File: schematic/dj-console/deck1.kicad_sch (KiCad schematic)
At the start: 111 parts, among them Q1 BC547, Q10 BC547, Q11 BC547, Q2 BC547, Q3 BC547, Q4 BC547, Q5 BC547, Q6 BC547, Q7 BC547, Q8 BC547, Q9 BC547, SW1_1 SW_Push, SW2_1 SW_Push, SW3_1 SW_Push, SW4_1 SW_Push, U2 MCP23017_SP, x1/2_IN_SW1 SW_Push, x2_OUT_SW1 SW_Push

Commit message: Added CD4013B to schematic
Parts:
- added U1, U3: ~, symbol D-flipflop:CD4013B
- C10, C12, C13, C14, C8, C9: value 1nF -> C
- R1: renamed from Rc1; value 520 -> R
- R1: renamed from Rb1; value 43kohm -> R
- R1, R11, R13, R3, R5, R7, R9: value 100k -> 100kOhm
- R10: renamed from Rc10; value 520 -> R
- R10, R12, R2, R4, R6, R8: value 12k -> 12kOhm
- R10: renamed from Rb10; value 43kohm -> R
- R11: renamed from Rb11; value 43kohm -> R
- R11: renamed from Rc11; value 520 -> R
- R14: value 12k -> 1nF
- R15, R17, R19, R23, R25, R27: value 100k -> R
- R16, R18, R20, R24, R26, R28: value 12k -> R
- R2: renamed from Rb2; value 43kohm -> R
- R2: renamed from Rc2; value 520 -> R
- R3: renamed from Rc3; value 520 -> R
- R3: renamed from Rb3; value 43kohm -> R
- R4: renamed from Rc4; value 520 -> R
- R4: renamed from Rb4; value 43kohm -> R
- R5: renamed from Rc5; value 520 -> R
- R5: renamed from Rb5; value 43kohm -> R
- R6: renamed from Rb6; value 43kohm -> R
- R6: renamed from Rc6; value 520 -> R
- R7: renamed from Rb7; value 43kohm -> R
- R7: renamed from Rc7; value 520 -> R
- R8: renamed from Rb8; value 43kohm -> R
- R8: renamed from Rc8; value 520 -> R
- R9: renamed from Rb9; value 43kohm -> R
- R9: renamed from Rc9; value 520 -> R
- SW2: renamed from CUE_SW1; value SW_Push -> CUE_SW1
- renumbered STEMS_SW1 to SW1, SYNC_SW1 to SW1, LOOP_SW1 to SW1, HOTCUE_SW1 to SW1, SHIFT_SW1 to SW1, x1/2_IN_SW1 to x1/2_IN_SW?, x2_OUT_SW1 to x2_OUT_SW?
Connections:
- net GND: now also U1.7 (VSS), U3.7 (VSS)
- net PLAY_SW1: now also U1.3 (CLK1), U3.3 (CLK1)
- net SYNC_SW1: now also U1.11 (CLK2), U3.11 (CLK2)
- new net PLAY_LED1: U1.1 (Q1), U3.1 (Q1)
- new net SYNC_LED1: U1.13 (Q2), U3.13 (Q2)
- new net ~{PLAY_LED1}: U1.2 (~{Q1}), U1.5 (D1), U3.2 (~{Q1}), U3.5 (D1)
- new net ~{SYNC_LED1}: U1.12 (~{Q2}), U1.9 (D2), U3.12 (~{Q2}), U3.9 (D2)
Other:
- note added: "Vce = 1V Ib = 100uA Ic = 20mA Rb = 43kohm Rc = 510"
- note removed: "Vce = 1V Ib = 100uA Ic = 20mA"
- moved on the sheet: C12, C13, C14, C8, D12, D13, D14, D8, R15, R16, R23, R24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

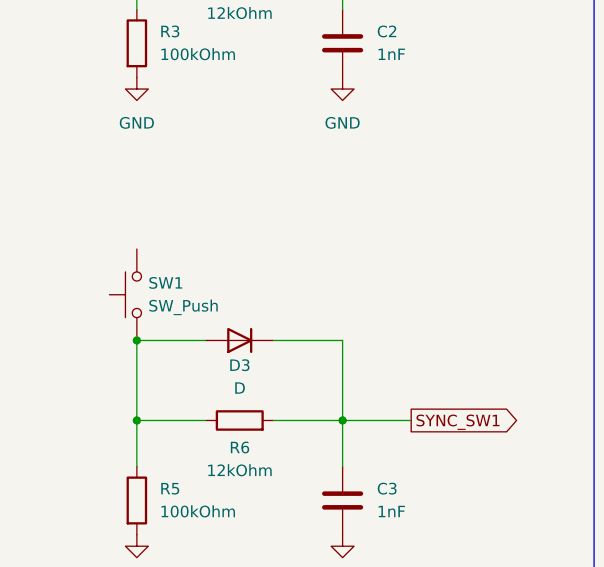
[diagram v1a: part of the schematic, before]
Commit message: Added CD4013B to schematic
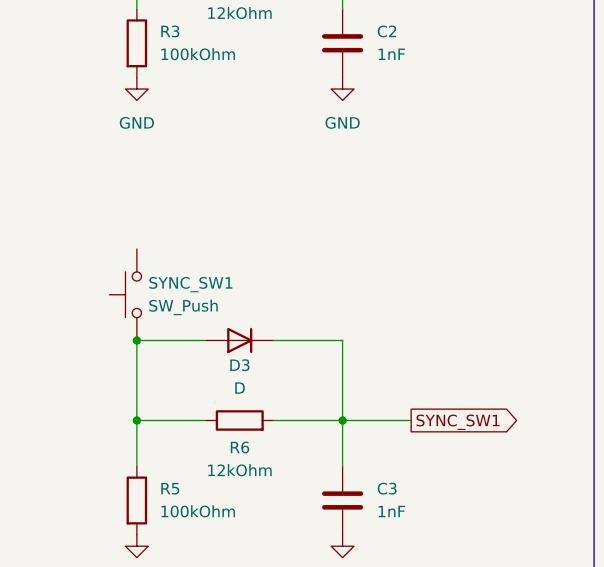
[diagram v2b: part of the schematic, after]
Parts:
- renumbered SW1 to SYNC_SW1
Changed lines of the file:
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@@
 		(dnp no)
 		(fields_autoplaced yes)
-		(property "Reference" "SW1"
+		(property "Reference" "SYNC_SW1"
 			(at 26.67 130.8099 90)
 			(effects
@@
 			(project "dj-console"
 				(path "/cbea8acf-e301-41c4-99fc-3eb7e47427af/a354910e-06bf-4bdc-8f1b-b82fc8536ab6"
-					(reference "SW1")
+					(reference "SYNC_SW1")
 					(unit 1)
 				)
@@
 		(dnp no)
 		(fields_autoplaced yes)
-		(property "Reference" "#PWR?"
+		(property "Reference" "#PWR0101"
 			(at 427.99 58.42 0)
 			(effects
@@
 			(project "dj-console"
 				(path "/cbea8acf-e301-41c4-99fc-3eb7e47427af/a354910e-06bf-4bdc-8f1b-b82fc8536ab6"
-					(reference "#PWR?")
+					(reference "#PWR0101")
 					(unit 1)
 				)
@@
 		(dnp no)
 		(fields_autoplaced yes)
-		(property "Reference" "#PWR?"
+		(property "Reference" "#PWR0102"
 			(at 427.99 100.33 0)
 			(effects
@@
 			(project "dj-console"
 				(path "/cbea8acf-e301-41c4-99fc-3eb7e47427af/a354910e-06bf-4bdc-8f1b-b82fc8536ab6"
-					(reference "#PWR?")
+					(reference "#PWR0102")
 					(unit 1)
 				)

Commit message: Connected switches for PADs controls to DFFs
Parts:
- removed U2: MCP23017_SP, Package_DIP:DIP-28_W7.62mm, symbol Interface_Expansion:MCP23017_SP
- added U4: MCP23017x-x-SP, Package_DIP:DIP-28_W7.62mm, symbol Interface_Expansion:MCP23017x-x-SP
- added U5, U6, U7: (no value), symbol D-flipflop:CD4013B
- U1, U3: value ~ -> (none)
- gave numbers to parts that had none: 2
- renumbered SW1 to HOT_CUE_SW1, SW1 to STEMS_SW1, SW2 to SW_Push, SW1 to x1-2_SW1, SW1 to x2_SW1
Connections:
- net CUE_SW1: now also U4.23 (GPA2)
- net GND: now also U4.10 (V_{SS}), U5.7 (VSS), U6.7 (VSS), U7.7 (VSS)
- net PLAY_LED1: now also U4.21 (GPA0), U7.1 (Q1); no longer U3.1 (Q1)
- net PLAY_SW1: now also U7.3 (CLK1); no longer U3.3 (CLK1)
- net SYNC_LED1: now also U4.22 (GPA1), U7.13 (Q2); no longer U3.13 (Q2)
- net SYNC_SW1: now also U7.11 (CLK2); no longer U3.11 (CLK2)
- net ~{PLAY_LED1}: now also U7.2 (~{Q1}), U7.5 (D1); no longer U3.2 (~{Q1}), U3.5 (D1)
- net ~{SYNC_LED1}: now also U7.12 (~{Q2}), U7.9 (D2); no longer U3.12 (~{Q2}), U3.9 (D2)
- net x2_SW1: now reaches C8.1, D8.1 (K), R16.2
- net x2_SW1: now also U6.11 (CLK2)
- net x1-2_SW1: now reaches C14.1, D14.1 (K), R28.2
- net x1-2_SW1: now also U6.3 (CLK1)
- net STEMS_SW1: now reaches C13.1, D13.1 (K), R26.2
- net STEMS_SW1: now also U5.11 (CLK2)
- net SHIFT_SW1: now reaches C10.1, D10.1 (K), R20.2
- net SHIFT_SW1: now also U3.11 (CLK2)
- net LOOP_SW1: now reaches C9.1, D9.1 (K), R18.2
- net LOOP_SW1: now also U3.3 (CLK1)
- net HOT_CUE_SW1: now reaches C12.1, D12.1 (K), R24.2
- net HOT_CUE_SW1: now also U5.3 (CLK1)
- new net HOT_CUE_LED1: U5.1 (Q1)
- new net LOOP_LED1: U3.1 (Q1)
- new net SHIFT_LED1: U3.13 (Q2)
- new net STEMS_LED1: U5.13 (Q2)
- new net x1-2_LED1: U6.1 (Q1)
- new net x2_LED1: U6.13 (Q2)
- new net ~{HOT_CUE_LED1}: U5.2 (~{Q1}), U5.5 (D1)
- new net ~{LOOP_LED1}: U3.2 (~{Q1}), U3.5 (D1)
- new net ~{SHIFT_LED1}: U3.12 (~{Q2}), U3.9 (D2)
- new net ~{STEMS_LED1}: U5.12 (~{Q2}), U5.9 (D2)
- new net ~{x1-2_LED1}: U6.2 (~{Q1}), U6.5 (D1)
- new net ~{x2_LED1}: U6.12 (~{Q2}), U6.9 (D2)
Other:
- moved on the sheet: C10, C12, C13, C14, C8, C9, D10, D11, D12, D13, D14, D15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

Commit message: Finished DECK circuitry -> to be reviewed; Created hierarchical sheets to avoid redundancy
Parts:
- removed D19: LED, symbol Device:LED
- removed Q6: BC547, Package_TO_SOT_THT:TO-92_Inline, symbol Transistor_BJT:BC547
- removed R10 (x2), R11 (x2), R3 (x2), R4 (x2), R5 (x2), R6 (x2), R7 (x2), R8 (x2), R9 (x2): R, symbol Device:R
- removed U7: (no value), symbol D-flipflop:CD4013B
- added C10, C11, C12, C37, C8, C9: 10uF, symbol Device:C_Polarized
- added D15, D25, D26: LED, symbol Device:LED
- added Q12, Q13, Q2: BC547, Package_TO_SOT_THT:TO-92_Inline, symbol Transistor_BJT:BC547
- added R28, R29, R30, R35, R37, R41, R42, R43, R47, R48, R49: 43kOhm, symbol Device:R
- added R32, R33, R34, R38, R40, R44, R45, R46, R50, R51, R52: 510Ohm, symbol Device:R
- added U1: LM741, symbol Amplifier_Operational:LM741
- added U7: (no value), symbol GPIO_expander:MCP23017
- C13: renamed from C9; value C -> 1nF
- C14: renamed from C10; value C -> 1nF
- C15: renamed from C12; value C -> 1nF
- C16: renamed from C13; value C -> 1nF
- C17: renamed from C14; value C -> 1nF
- C18: renamed from C8; value C -> 1nF
- R15: renamed from R17; value R -> 100kOhm
- R16: renamed from R19; value R -> 100kOhm
- R17: renamed from R23; value R -> 100kOhm
- R18: renamed from R25; value R -> 100kOhm
- R19: renamed from R27; value R -> 10kOhm
- R20: renamed from R15; value R -> 100kOhm
- R21: renamed from R18; value R -> 12kOhm
- R22: renamed from R20; value R -> 12kOhm
- R23: renamed from R24; value R -> 12kOhm
- R24: renamed from R26; value R -> 12kOhm
- R25: renamed from R28; value R -> 12kOhm
- R26: renamed from R16; value R -> 12kOhm
- R27: renamed from R1; value R -> 43kOhm
- R31: renamed from R1; value R -> 510Ohm
- R36: renamed from R2; value R -> 43kOhm
- R39: renamed from R2; value R -> 510Ohm
- SW_Push: value CUE_SW1 -> CUE_SW
- renumbered D12 to D10, D13 to D11, D14 to D12, D8 to D13, D11 to D14, D15 to D19, D9 to D8, D10 to D9, Q2 to Q6, R6 to R10, R8 to R11, R10 to R12, R12 to R13, R3 to R2, R5 to R3, R7 to R4, R9 to R5, R11 to R6, R13 to R7, R2 to R8, R4 to R9, SW1_1 to SW1, SW2_1 to SW2, SW3_1 to SW3, SW4_1 to SW4, U4 to U2, U1 to U3, U3 to U4, U1 to U8
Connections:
- net HOT_CUE_LED1 is gone; now on net HOT_CUE_LED: U5.1 (Q1)
- net LOOP_LED1 is gone; now on net LOOP_LED: U4.1 (Q1)
- net PLAY_LED1 is gone; now on net PLAY_LED: U2.21 (GPA0), U3.1 (Q1)
- net SHIFT_LED1 is gone; now on net SHIFT_LED: U4.13 (Q2)
- net STEMS_LED1 is gone; now on net STEMS_LED: U5.13 (Q2)
- net SW2_1 is gone; now on net SW2: C5.1, D5.1 (K), R12.2
- net SW3_1 is gone; now on net SW3: C6.1, D6.1 (K), R13.2
- net SW4_1 is gone; now on net SW4: C7.1, D7.1 (K), R14.2
- net x1-2_LED1 is gone; now on net x1-2_LED: U6.1 (Q1)
- net x2_LED1 is gone; now on net x2_LED: U6.13 (Q2)
- net +12V: now also R32.1, R33.1, R34.1, R38.1, R40.1, R44.1, R45.1, R46.1, R50.1, R51.1, R52.1
- net GND: now also C10.2, C11.2, C12.2, C8.2, C9.2, Q12.3 (E), Q13.3 (E), Q2.3 (E), U1.4 (V-)
- net +5V: now reaches STEMS_SW1.2
- net +5V: now also HOT_CUE_SW1.2, LOOP_SW1.2, PLAY_SW1.2, SHIFT_SW1.2, SW1.2, SW2.2, SW3.2, SW4.2, SW_Push.2, SYNC_SW1.2, U2.9 (V_{DD}), U3.14 (VDD), U4.14 (VDD), U5.14 (VDD), U6.14 (VDD), x1-2_SW1.2, x2_SW1.2, C10.1, C11.1, C12.1, C37.1, C8.1, C9.1, U1.7 (V+)
- net at D20.2 (A): now also R40.2
- net CUE_LED: now reaches R36.1
- net CUE_LED: now also U1.2 (-), U1.6
- net at Q3.2 (B): now also R29.2
- net at D24.2 (A): now also R50.2
- net at Q7.2 (B): now also R37.2
- net at Q9.2 (B): now also R42.2
- net at D16.2 (A): now also R33.2
- net at D23.2 (A): now also R46.2
- net at D21.2 (A): now also R44.2
- net at Q8.2 (B): now also R41.2
- net at Q11.2 (B): now also R47.2
- net at Q5.2 (B): now also R35.2
- net at Q4.2 (B): now also R30.2
- net at D22.2 (A): now also R45.2
- net at D18.2 (A): now also R38.2
- net PLAY_LED: now reaches R27.1
- net at D17.2 (A): now also R34.2
- net at Q10.2 (B): now also R43.2
- net LOOP_LED: now reaches U2.1 (GPB0)
- net LOOP_LED: now also R41.1
- net SHIFT_LED: now reaches U2.2 (GPB1)
- net SHIFT_LED: now also R47.1
- net SW1: now reaches U2.24 (GPA3)
- net SW2: now reaches U2.25 (GPA4)
- net SW3: now reaches U2.26 (GPA5)
- net SW4: now reaches U2.27 (GPA6)
- net HOT_CUE_LED: now reaches U2.3 (GPB2)
- net HOT_CUE_LED: now also R42.1
- net STEMS_LED: now reaches U2.4 (GPB3)
- net STEMS_LED: now also R48.1
- net x1-2_LED: now reaches U2.5 (GPB4)
- net x1-2_LED: now also R43.1
- net x2_LED: now reaches U2.6 (GPB5)
- net x2_LED: now also R49.1
- net CUE_SW1 renamed CUE_SW
- net CUE_SW: now also U1.3 (+)
- net HOT_CUE_SW1 renamed HOT_CUE_SW
- net LOOP_SW1 renamed LOOP_SW
- net PLAY_SW1 renamed PLAY_SW
- net SHIFT_SW1 renamed SHIFT_SW
- net STEMS_SW1 renamed STEMS_SW
- net SYNC_LED1 renamed SYNC_LED
- net SYNC_LED: now also R28.1
- net SYNC_SW1 renamed SYNC_SW
- net x1-2_SW1 renamed x1-2_SW
- net x2_SW1 renamed x2_SW
- net ~{HOT_CUE_LED1} renamed ~{HOT_CUE_LED}
- net ~{LOOP_LED1} renamed ~{LOOP_LED}
- net ~{PLAY_LED1} renamed ~{PLAY_LED}
- net ~{SHIFT_LED1} renamed ~{SHIFT_LED}
- net ~{STEMS_LED1} renamed ~{STEMS_LED}
- net ~{SYNC_LED1} renamed ~{SYNC_LED}
- net ~{x1-2_LED1} renamed ~{x1-2_LED}
- net ~{x2_LED1} renamed ~{x2_LED}
- new net: D26.1 (K), Q13.1 (C)
- new net: Q13.2 (B), R49.2
- new net: D15.1 (K), Q2.1 (C)
- new net: D15.2 (A), R32.2
- new net: D26.2 (A), R52.2
- new net: Q2.2 (B), R28.2
- new net: D25.1 (K), Q12.1 (C)
- new net: D25.2 (A), R51.2
- new net: Q12.2 (B), R48.2
- new net SW1_LED: R29.1
- new net SW2_LED: R35.1
- new net SW3_LED: R30.1
- new net SW4_LED: R37.1
- no-connect marks 11 -> 13

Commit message: Created first version of mixer circuit and added tempo sliders on decks
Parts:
- removed SW_Push: CUE_SW, symbol Switch:SW_Push
- added C67: C, symbol Device:C
- added C68: 10uF, symbol Device:C_Polarized
- added CUE_SW1: SW_Push, symbol Switch:SW_Push
- added R31, R36: R, symbol Device:R
- added TEMPO_SLIDER1: 100kOhm, symbol Device:R_Potentiometer
- added U31: LM741, symbol Amplifier_Operational:LM741
- renumbered C9 to C10, C10 to C11, C11 to C12, C12 to C13, C13 to C14, C14 to C15, C15 to C16, C16 to C17, C17 to C18, C18 to C19, C37 to C9, R51 to R125, R52 to R126, R31 to R32, R32 to R33, R33 to R34, R34 to R35, R35 to R37, R36 to R38, R37 to R39, R38 to R40, R39 to R41, R40 to R42, R41 to R43, R42 to R44, R43 to R45, R44 to R46, R45 to R47, R46 to R48, R47 to R49, R48 to R50, R49 to R51, R50 to R52, SW1 to SW1_1, SW2 to SW2_1, SW3 to SW3_1, SW4 to SW4_1
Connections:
- net +12V: now also C9.1, U1.7 (V+), C68.1, U31.7 (V+)
- net +5V: now also CUE_SW1.2, TEMPO_SLIDER1.1; no longer C9.1, U1.7 (V+)
- net GND: now also C9.2, C68.2, TEMPO_SLIDER1.3, U31.3 (+), U31.4 (V-)
- net at D2.2 (A), R2.1, R9.1: now also CUE_SW1.1
- net HEADPHONES_STAT: now reaches U2.7 (GPB6)
- new net: R31.1, TEMPO_SLIDER1.2
- new net: C67.2, R31.2, R36.1, U31.2 (-)
- new net TEMPO_SLIDER_filtered: C67.1, R36.2, U31.6
- no-connect marks 13 -> 17
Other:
- moved on the sheet: C14, C15, C16, C17, C18, C19, C9, D10, D11, D12, D13, D8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

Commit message: Added MASTER and HEADPHONES gain together with crossfader slider
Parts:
- TEMPO_SLIDER1: value 100kOhm -> 10kOhm
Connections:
- net SW1_1 is gone; now on net SW1: C4.1, D4.1 (K), R11.2
- no-connect marks 17 -> 4
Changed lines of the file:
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@@
 	)
 	(no_connect
-		(at 474.98 193.04)
-	)
-	(no_connect
-		(at 349.25 116.84)
-	)
-	(no_connect
-		(at 474.98 52.07)
-	)
-	(no_connect
-		(at 347.98 52.07)
-	)
-	(no_connect
-		(at 411.48 193.04)
-	)
-	(no_connect
-		(at 349.25 193.04)
-	)
-	(no_connect
-		(at 474.98 116.84)
-	)
-	(no_connect
-		(at 412.75 52.07)
-	)
-	(no_connect
-		(at 353.06 278.13)
-	)
-	(no_connect
 		(at 373.38 363.22)
 	)
@@
 		(at 140.97 378.46)
 	)
-	(no_connect
-		(at 551.18 52.07)
-	)
-	(no_connect
-		(at 551.18 193.04)
-	)
-	(no_connect
-		(at 551.18 116.84)
-	)
-	(no_connect
-		(at 415.29 278.13)
-	)
 	(wire
 		(pts
@@
 		)
 	)
-	(label "SW1_1"
+	(label "SW1"
 		(at 55.88 222.25 180)
 		(effects
@@
 			)
 		)
-		(property "Value" "100kOhm"
+		(property "Value" "10kOhm"
 			(at 331.47 359.4099 0)
 			(show_name no)
@@
 	(symbol
 		(lib_id "GPIO_expander:MCP23017")
-		(at 275.59 167.64 0)
+		(at 279.4 170.18 0)
 		(unit 1)
 		(body_style 1)
@@
 		(fields_autoplaced yes)
 		(property "Reference" "U8"
-			(at 287.782 154.432 0)
+			(at 291.592 156.972 0)
 			(hide yes)
 			(show_name no)
@@
 		)
 		(property "Value" ""
-			(at 276.86 167.6399 0)
+			(at 280.67 170.1799 0)
 			(hide yes)
 			(show_name no)
@@
 		)
 		(property "Footprint" ""
-			(at 275.59 167.64 0)
+			(at 279.4 170.18 0)
 			(hide yes)
 			(show_name no)
@@
 		)
 		(property "Datasheet" ""
-			(at 275.59 167.64 0)
+			(at 279.4 170.18 0)
 			(hide yes)
 			(show_name no)
@@
 		)
 		(property "Description" ""
-			(at 275.59 167.64 0)
+			(at 279.4 170.18 0)
 			(hide yes)
 			(show_name no)

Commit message: Changed filtering circuit for knobs
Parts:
- removed C68: 10uF, symbol Device:C_Polarized
- removed R36: R, symbol Device:R
- added C69: 0.1uF, symbol Device:C_Polarized
- C10, C11, C12, C13, C9: value 10uF -> 0.1uF
- C67: value C -> 4.7nF
- R31: value R -> 8.2kOhm
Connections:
- net +12V: now also C69.1
- net GND: now also C67.2, C69.2; no longer U31.3 (+)
- net TEMPO_SLIDER_filtered: now also U31.2 (-); no longer C67.1
- new net: C67.1, R31.2, U31.3 (+)
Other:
- moved on the sheet: TEMPO_SLIDER1

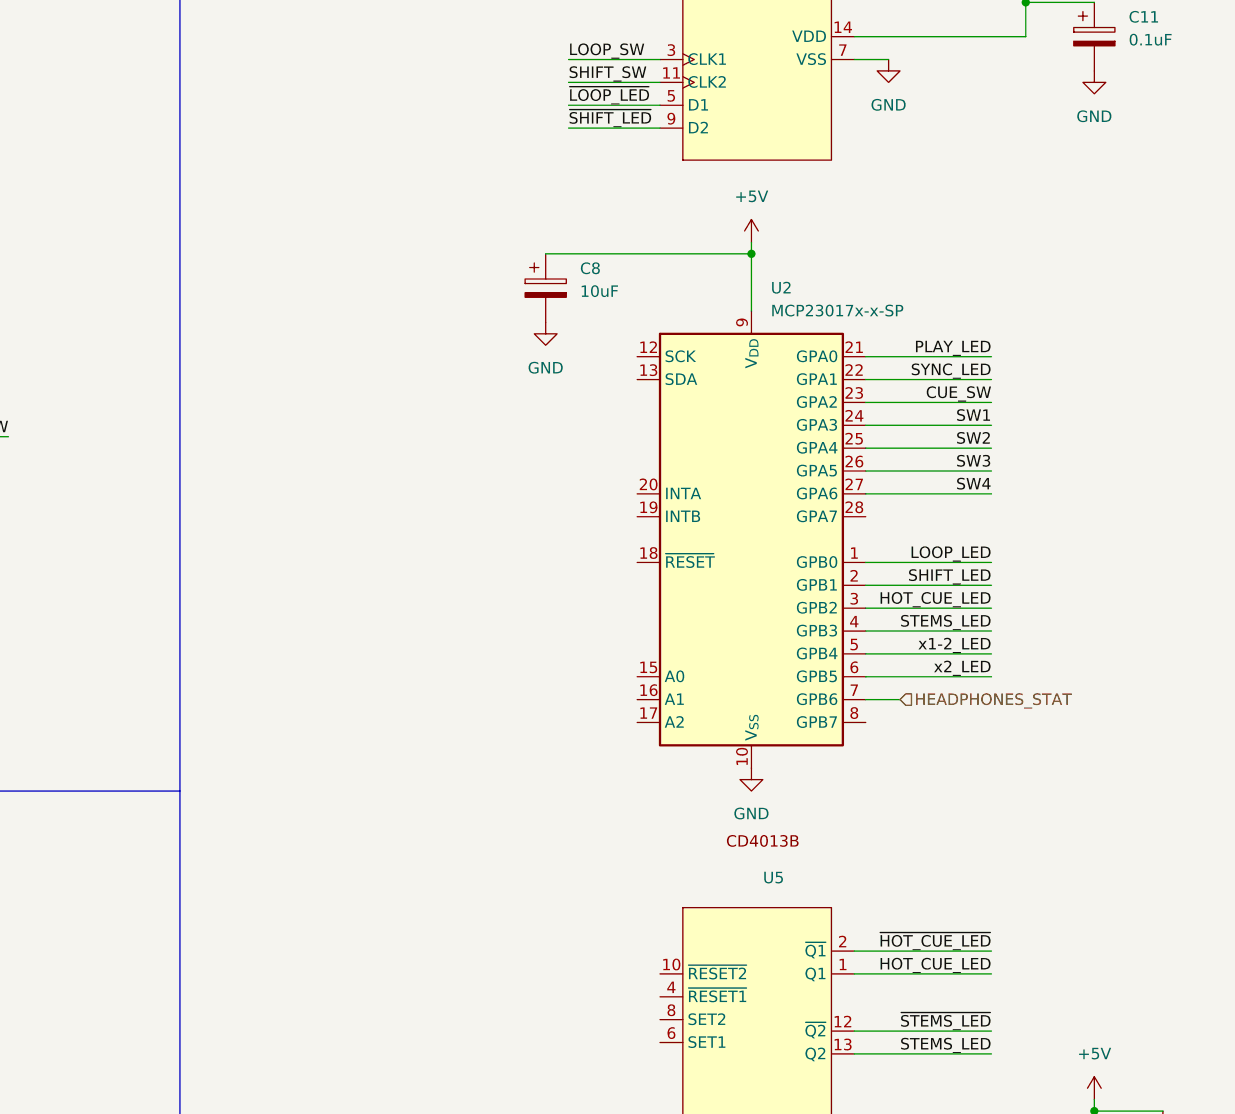
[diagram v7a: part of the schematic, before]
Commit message: Added I2C and SPI busses
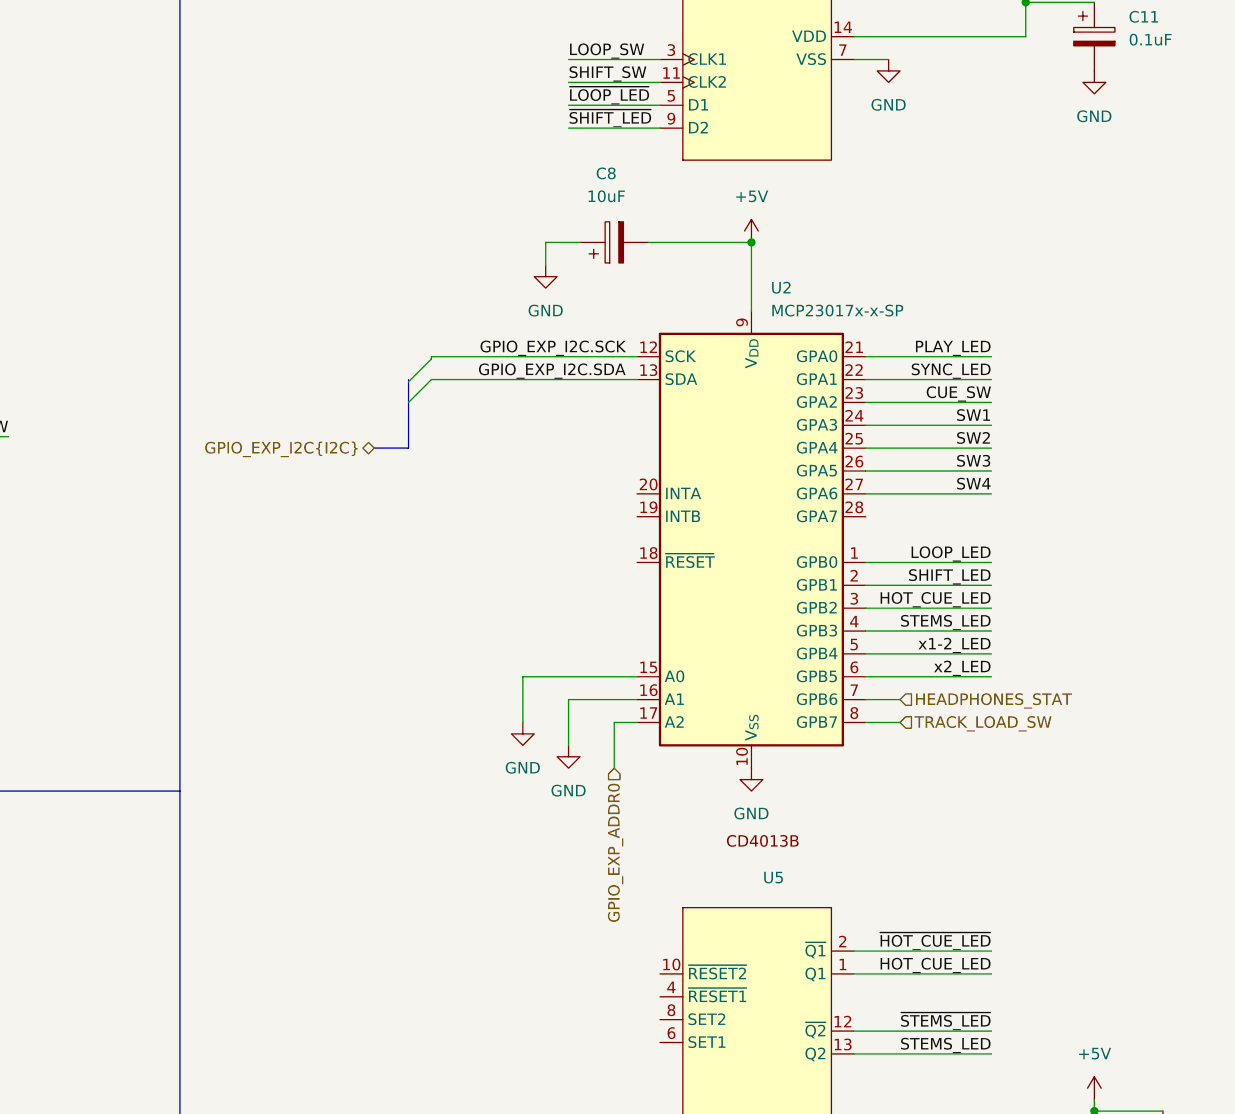
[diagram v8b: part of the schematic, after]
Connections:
- net +5V: now also C8.2; no longer C8.1
- net GND: now also C8.1, U2.15 (A0), U2.16 (A1); no longer C8.2
- net GPIO_EXP_I2C.SCK: now reaches U2.12 (SCK)
- net GPIO_EXP_I2C.SDA: now reaches U2.13 (SDA)
- net GPIO_EXP_ADDR0: now reaches U2.17 (A2)
- net TRACK_LOAD_SW: now reaches U2.8 (GPB7)
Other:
- moved on the sheet: C8
